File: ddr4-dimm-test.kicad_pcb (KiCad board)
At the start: 2 copper layers, 133.3 x 31.2 mm, 1 part

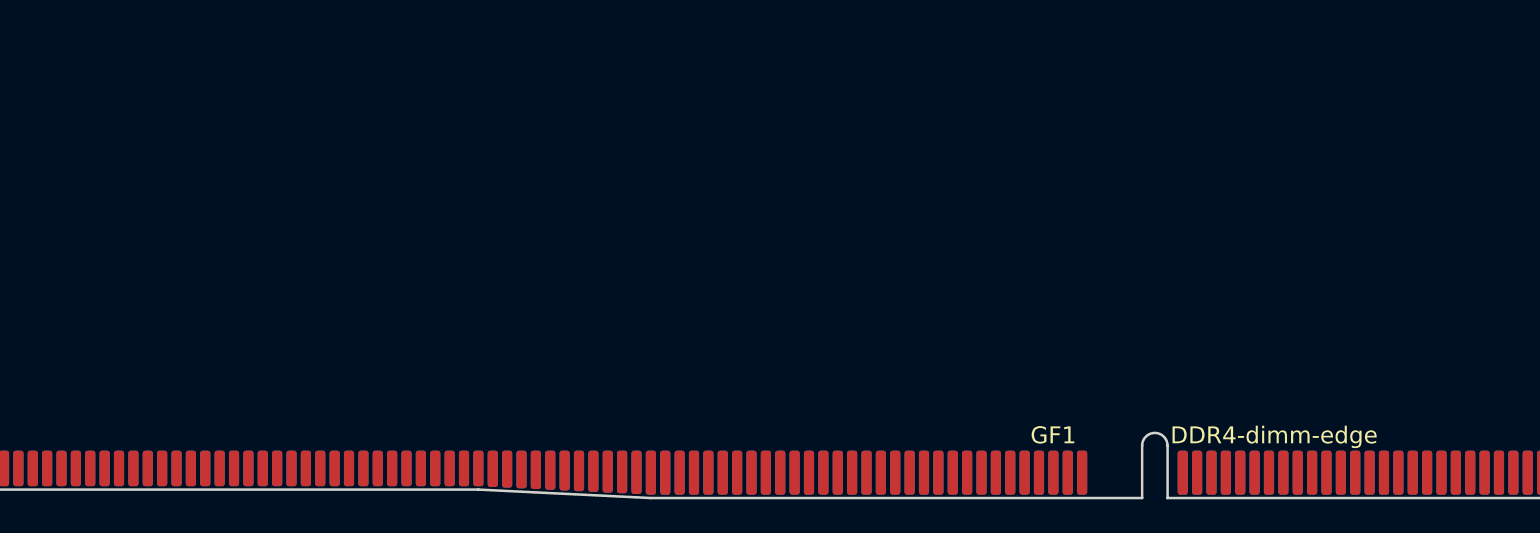
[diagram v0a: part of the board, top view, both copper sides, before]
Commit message: Added ram chip symbol and partial connections
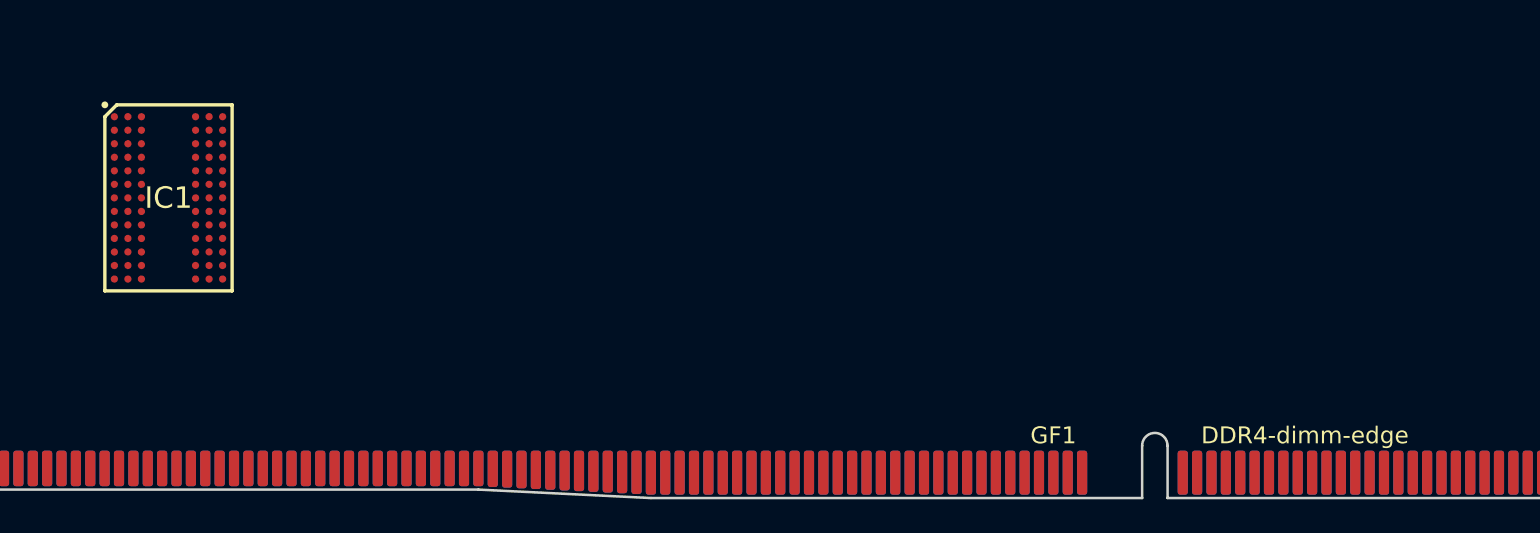
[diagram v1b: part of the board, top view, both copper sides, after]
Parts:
- added IC1: DDR4-BGA78, A_my_stuff:DDR4-BGA78, F.Cu at (89.3, 94.2)
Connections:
- GF1 pad 210: unconnected-(GF1-A11-Pad210) -> A11
- GF1 pad 211: unconnected-(GF1-A7-Pad211) -> A7
- GF1 pad 213: unconnected-(GF1-A5-Pad213) -> A5
- GF1 pad 214: unconnected-(GF1-A4-Pad214) -> A4
- GF1 pad 216: unconnected-(GF1-A2-Pad216) -> A2
- GF1 pad 224: unconnected-(GF1-BA1-Pad224) -> BA1
- GF1 pad 225: unconnected-(GF1-A10/AP-Pad225) -> A10
- GF1 pad 228: unconnected-(GF1-A14/WE#-Pad228) -> A14
- GF1 pad 232: unconnected-(GF1-A13-Pad232) -> A13
- GF1 pad 65: unconnected-(GF1-A12/BC#-Pad65) -> A12
- GF1 pad 66: unconnected-(GF1-A9-Pad66) -> A9
- GF1 pad 68: unconnected-(GF1-A8-Pad68) -> A8
- GF1 pad 69: unconnected-(GF1-A6-Pad69) -> A6
- GF1 pad 71: unconnected-(GF1-A3-Pad71) -> A3
- GF1 pad 72: unconnected-(GF1-A1-Pad72) -> A1
- GF1 pad 79: unconnected-(GF1-A0-Pad79) -> A0
- GF1 pad 81: unconnected-(GF1-BA0-Pad81) -> BA0
- GF1 pad 82: unconnected-(GF1-A16/RAS#-Pad82) -> A16
- GF1 pad 86: unconnected-(GF1-A15/CAS#-Pad86) -> A15

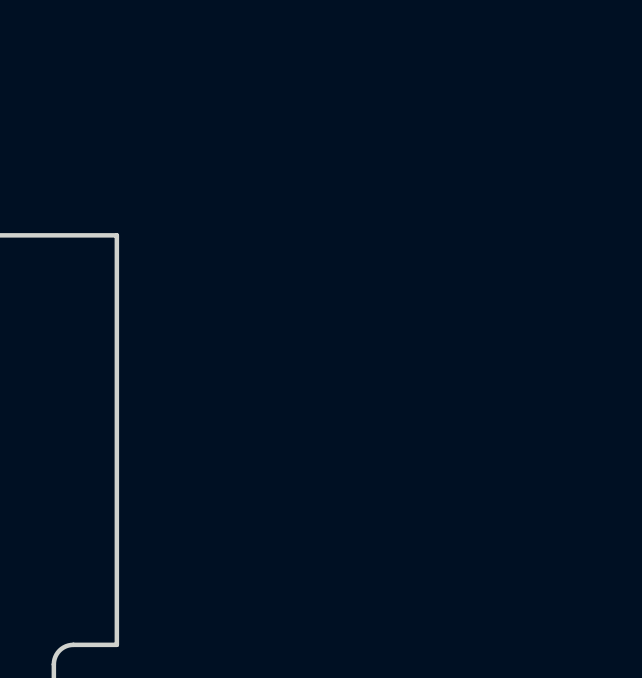
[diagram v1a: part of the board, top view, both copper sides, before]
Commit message: Connected all common lines and duplicated chip
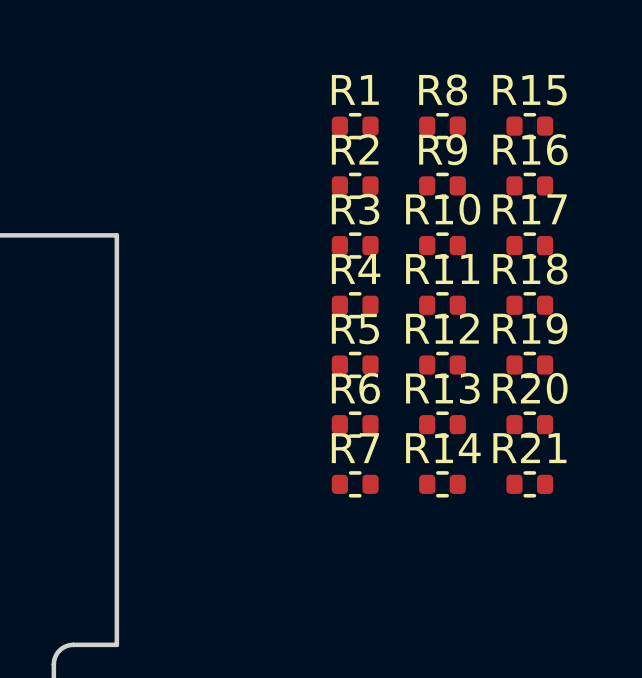
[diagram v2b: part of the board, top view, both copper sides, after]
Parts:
- added R1: 39Ω, Resistor_SMD:R_0402_1005Metric, F.Cu at (216.7, 77.1)
- added R10: 39Ω, Resistor_SMD:R_0402_1005Metric, F.Cu at (219.6, 81.0)
- added R11: 39Ω, Resistor_SMD:R_0402_1005Metric, F.Cu at (219.6, 83.0)
- added R12: 39Ω, Resistor_SMD:R_0402_1005Metric, F.Cu at (219.6, 85.0)
- added R13: 39Ω, Resistor_SMD:R_0402_1005Metric, F.Cu at (219.6, 87.0)
- added R14: 39Ω, Resistor_SMD:R_0402_1005Metric, F.Cu at (219.6, 89.0)
- added R15: 39Ω, Resistor_SMD:R_0402_1005Metric, F.Cu at (222.5, 77.1)
- added R16: 39Ω, Resistor_SMD:R_0402_1005Metric, F.Cu at (222.5, 79.0)
- added R17: 39Ω, Resistor_SMD:R_0402_1005Metric, F.Cu at (222.5, 81.0)
- added R18: 39Ω, Resistor_SMD:R_0402_1005Metric, F.Cu at (222.5, 83.0)
- added R19: 39Ω, Resistor_SMD:R_0402_1005Metric, F.Cu at (222.5, 85.0)
- added R2: 39Ω, Resistor_SMD:R_0402_1005Metric, F.Cu at (216.7, 79.0)
- added R20: 39Ω, Resistor_SMD:R_0402_1005Metric, F.Cu at (222.5, 87.0)
- added R21: 39Ω, Resistor_SMD:R_0402_1005Metric, F.Cu at (222.5, 89.0)
- added R3: 39Ω, Resistor_SMD:R_0402_1005Metric, F.Cu at (216.7, 81.0)
- added R4: 39Ω, Resistor_SMD:R_0402_1005Metric, F.Cu at (216.7, 83.0)
- added R5: 39Ω, Resistor_SMD:R_0402_1005Metric, F.Cu at (216.7, 85.0)
- added R6: 39Ω, Resistor_SMD:R_0402_1005Metric, F.Cu at (216.7, 87.0)
- added R7: 39Ω, Resistor_SMD:R_0402_1005Metric, F.Cu at (216.7, 89.0)
- added R8: 39Ω, Resistor_SMD:R_0402_1005Metric, F.Cu at (219.6, 77.1)
- added R9: 39Ω, Resistor_SMD:R_0402_1005Metric, F.Cu at (219.6, 79.0)
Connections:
- GF1 pad 146: unconnected-(GF1-VREFCA-Pad146) -> VREFCA
- GF1 pad 207: unconnected-(GF1-BG1-Pad207) -> BG1
- GF1 pad 63: unconnected-(GF1-BG0-Pad63) -> BG0
- GF1 pad 74: unconnected-(GF1-CK0+-Pad74) -> CK0+
- GF1 pad 75: unconnected-(GF1-CK0--Pad75) -> CK0-
- IC1 pad A1: unconnected-(IC1-VDD_1-PadA1) -> VDD
- IC1 pad A2: unconnected-(IC1-VSSQ_1-PadA2) -> GND
- IC1 pad A8: unconnected-(IC1-VSSQ_2-PadA8) -> GND
- IC1 pad A9: unconnected-(IC1-VSS_1-PadA9) -> GND
- IC1 pad B1: unconnected-(IC1-VPP_1-PadB1) -> VPP
- IC1 pad B2: unconnected-(IC1-VDDQ_1-PadB2) -> VDD
- IC1 pad B8: unconnected-(IC1-VDDQ_2-PadB8) -> VDD
- IC1 pad C1: unconnected-(IC1-VDDQ_3-PadC1) -> VDD
- IC1 pad C7: unconnected-(IC1-VDD_2-PadC7) -> VDD
- IC1 pad C8: unconnected-(IC1-VSS_2-PadC8) -> GND
- IC1 pad C9: unconnected-(IC1-VDDQ_4-PadC9) -> VDD
- IC1 pad D1: unconnected-(IC1-VSSQ_3-PadD1) -> GND
- IC1 pad D9: unconnected-(IC1-VSSQ_4-PadD9) -> GND
- IC1 pad E1: unconnected-(IC1-VSS_3-PadE1) -> GND
- IC1 pad E2: unconnected-(IC1-VDDQ_5-PadE2) -> VDD
- IC1 pad E8: unconnected-(IC1-VDDQ_6-PadE8) -> VDD
- IC1 pad E9: unconnected-(IC1-VSS_4-PadE9) -> GND
- IC1 pad F1: unconnected-(IC1-VDD_3-PadF1) -> VDD
- IC1 pad F7: unconnected-(IC1-CK+-PadF7) -> CK0+
- IC1 pad F8: unconnected-(IC1-CK--PadF8) -> CK0-
- IC1 pad F9: unconnected-(IC1-VDD_4-PadF9) -> VDD
- IC1 pad G1: unconnected-(IC1-VSS_5-PadG1) -> GND
- IC1 pad H1: unconnected-(IC1-VDD_5-PadH1) -> VDD
- IC1 pad H9: unconnected-(IC1-VSS_6-PadH9) -> GND
- IC1 pad J1: unconnected-(IC1-VREFCA-PadJ1) -> VREFCA
- IC1 pad J2: unconnected-(IC1-BG0-PadJ2) -> BG0
- IC1 pad J8: unconnected-(IC1-BG1-PadJ8) -> BG1
- IC1 pad J9: unconnected-(IC1-VDD_6-PadJ9) -> VDD
- IC1 pad K1: unconnected-(IC1-VSS_7-PadK1) -> GND
- IC1 pad K9: unconnected-(IC1-VSS_8-PadK9) -> GND
- IC1 pad M1: unconnected-(IC1-VDD_7-PadM1) -> VDD
- IC1 pad M9: unconnected-(IC1-VPP_2-PadM9) -> VPP
- IC1 pad N1: unconnected-(IC1-VSS_9-PadN1) -> GND
- IC1 pad N9: unconnected-(IC1-VDD_8-PadN9) -> VDD

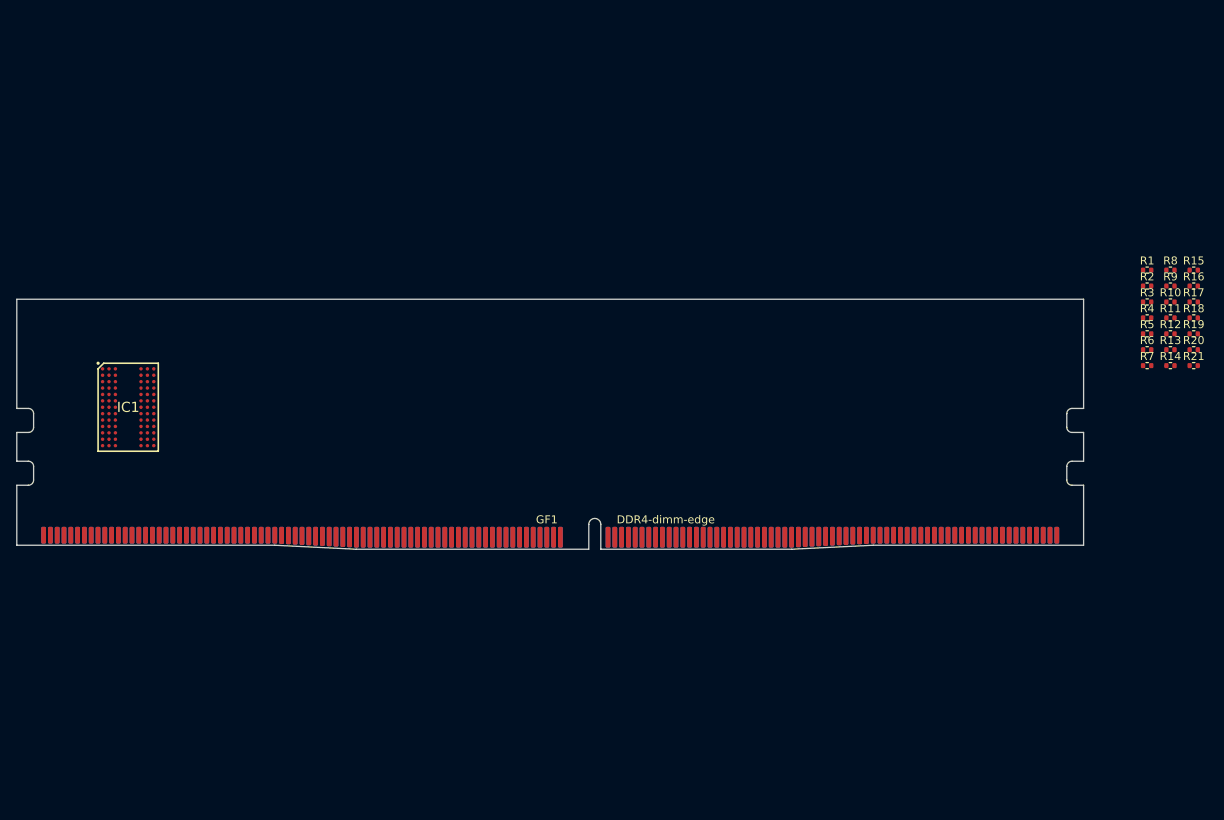
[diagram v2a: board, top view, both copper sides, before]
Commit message: Connected data bus
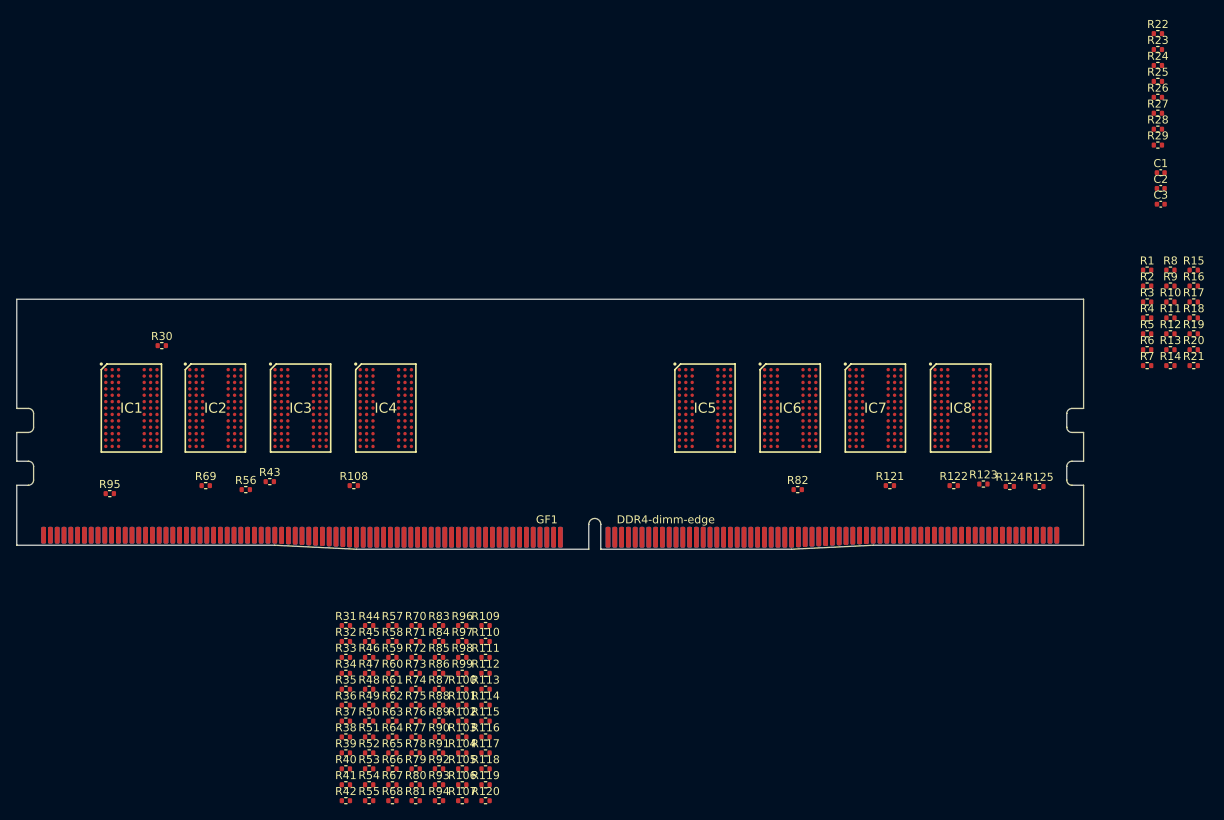
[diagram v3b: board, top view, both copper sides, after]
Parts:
- added C1: 0.01uF, Capacitor_SMD:C_0402_1005Metric, F.Cu at (218.4, 64.9)
- added C2: ?, Capacitor_SMD:C_0402_1005Metric, F.Cu at (218.4, 66.8)
- added C3: 10pF, Capacitor_SMD:C_0402_1005Metric, F.Cu at (218.4, 68.8)
- added IC2: DDR4-BGA78, A_my_stuff:DDR4-BGA78, F.Cu at (100.2, 94.3)
- added IC3: DDR4-BGA78, A_my_stuff:DDR4-BGA78, F.Cu at (110.8, 94.3)
- added IC4: DDR4-BGA78, A_my_stuff:DDR4-BGA78, F.Cu at (121.5, 94.3)
- added IC5: DDR4-BGA78, A_my_stuff:DDR4-BGA78, F.Cu at (161.4, 94.3)
- added IC6: DDR4-BGA78, A_my_stuff:DDR4-BGA78, F.Cu at (172.1, 94.3)
- added IC7: DDR4-BGA78, A_my_stuff:DDR4-BGA78, F.Cu at (182.7, 94.3)
- added IC8: DDR4-BGA78, A_my_stuff:DDR4-BGA78, F.Cu at (193.3, 94.3)
- added R100: 15Ω, Resistor_SMD:R_0402_1005Metric, F.Cu at (131.1, 129.4)
- added R101: 15Ω, Resistor_SMD:R_0402_1005Metric, F.Cu at (131.1, 131.4)
- added R102: 15Ω, Resistor_SMD:R_0402_1005Metric, F.Cu at (131.1, 133.4)
- added R103: 15Ω, Resistor_SMD:R_0402_1005Metric, F.Cu at (131.1, 135.4)
- added R104: 15Ω, Resistor_SMD:R_0402_1005Metric, F.Cu at (131.1, 137.4)
- added R105: 15Ω, Resistor_SMD:R_0402_1005Metric, F.Cu at (131.1, 139.4)
- added R106: 15Ω, Resistor_SMD:R_0402_1005Metric, F.Cu at (131.1, 141.4)
- added R107: 15Ω, Resistor_SMD:R_0402_1005Metric, F.Cu at (131.1, 143.4)
- added R108: 15Ω, Resistor_SMD:R_0402_1005Metric, F.Cu at (117.5, 104.0)
- added R109: 15Ω, Resistor_SMD:R_0402_1005Metric, F.Cu at (134.0, 121.5)
- added R110: 15Ω, Resistor_SMD:R_0402_1005Metric, F.Cu at (134.0, 123.5)
- added R111: 15Ω, Resistor_SMD:R_0402_1005Metric, F.Cu at (134.0, 125.5)
- added R112: 15Ω, Resistor_SMD:R_0402_1005Metric, F.Cu at (134.0, 127.5)
- added R113: 15Ω, Resistor_SMD:R_0402_1005Metric, F.Cu at (134.0, 129.4)
- added R114: 15Ω, Resistor_SMD:R_0402_1005Metric, F.Cu at (134.0, 131.4)
- added R115: 15Ω, Resistor_SMD:R_0402_1005Metric, F.Cu at (134.0, 133.4)
- added R116: 15Ω, Resistor_SMD:R_0402_1005Metric, F.Cu at (134.0, 135.4)
- added R117: 15Ω, Resistor_SMD:R_0402_1005Metric, F.Cu at (134.0, 137.4)
- added R118: 15Ω, Resistor_SMD:R_0402_1005Metric, F.Cu at (134.0, 139.4)
- added R119: 15Ω, Resistor_SMD:R_0402_1005Metric, F.Cu at (134.0, 141.4)
- added R120: 15Ω, Resistor_SMD:R_0402_1005Metric, F.Cu at (134.0, 143.4)
- added R121: 15Ω, Resistor_SMD:R_0402_1005Metric, F.Cu at (184.5, 104.0)
- added R122: 15Ω, Resistor_SMD:R_0402_1005Metric, F.Cu at (192.5, 104.0)
- added R123: 15Ω, Resistor_SMD:R_0402_1005Metric, F.Cu at (196.2, 103.8)
- added R124: 15Ω, Resistor_SMD:R_0402_1005Metric, F.Cu at (199.5, 104.1)
- added R125: 15Ω, Resistor_SMD:R_0402_1005Metric, F.Cu at (203.2, 104.1)
- added R22: 39Ω, Resistor_SMD:R_0402_1005Metric, F.Cu at (218.0, 47.5)
- added R23: 39Ω, Resistor_SMD:R_0402_1005Metric, F.Cu at (218.0, 49.5)
- added R24: 39Ω, Resistor_SMD:R_0402_1005Metric, F.Cu at (218.0, 51.5)
- added R25: 39Ω, Resistor_SMD:R_0402_1005Metric, F.Cu at (218.0, 53.5)
- added R26: 39Ω, Resistor_SMD:R_0402_1005Metric, F.Cu at (218.0, 55.5)
- added R27: 39Ω, Resistor_SMD:R_0402_1005Metric, F.Cu at (218.0, 57.5)
- added R28: 39Ω, Resistor_SMD:R_0402_1005Metric, F.Cu at (218.0, 59.4)
- added R29: 47Ω, Resistor_SMD:R_0402_1005Metric, F.Cu at (218.0, 61.4)
- added R30: 240Ω, Resistor_SMD:R_0402_1005Metric, F.Cu at (93.5, 86.5)
- added R31: 240Ω, Resistor_SMD:R_0402_1005Metric, F.Cu at (116.5, 121.5)
- added R32: 240Ω, Resistor_SMD:R_0402_1005Metric, F.Cu at (116.5, 123.5)
- added R33: 240Ω, Resistor_SMD:R_0402_1005Metric, F.Cu at (116.5, 125.5)
- added R34: 240Ω, Resistor_SMD:R_0402_1005Metric, F.Cu at (116.5, 127.5)
- added R35: 240Ω, Resistor_SMD:R_0402_1005Metric, F.Cu at (116.5, 129.4)
- added R36: 240Ω, Resistor_SMD:R_0402_1005Metric, F.Cu at (116.5, 131.4)
- added R37: 240Ω, Resistor_SMD:R_0402_1005Metric, F.Cu at (116.5, 133.4)
- added R38: 15Ω, Resistor_SMD:R_0402_1005Metric, F.Cu at (116.5, 135.4)
- added R39: 15Ω, Resistor_SMD:R_0402_1005Metric, F.Cu at (116.5, 137.4)
- added R40: 15Ω, Resistor_SMD:R_0402_1005Metric, F.Cu at (116.5, 139.4)
- added R41: 15Ω, Resistor_SMD:R_0402_1005Metric, F.Cu at (116.5, 141.4)
- added R42: 15Ω, Resistor_SMD:R_0402_1005Metric, F.Cu at (116.5, 143.4)
- added R43: 15Ω, Resistor_SMD:R_0402_1005Metric, F.Cu at (107.0, 103.5)
- added R44: 15Ω, Resistor_SMD:R_0402_1005Metric, F.Cu at (119.4, 121.5)
- added R45: 15Ω, Resistor_SMD:R_0402_1005Metric, F.Cu at (119.4, 123.5)
- added R46: 15Ω, Resistor_SMD:R_0402_1005Metric, F.Cu at (119.4, 125.5)
- added R47: 15Ω, Resistor_SMD:R_0402_1005Metric, F.Cu at (119.4, 127.5)
- added R48: 15Ω, Resistor_SMD:R_0402_1005Metric, F.Cu at (119.4, 129.4)
- added R49: 15Ω, Resistor_SMD:R_0402_1005Metric, F.Cu at (119.4, 131.4)
- added R50: 15Ω, Resistor_SMD:R_0402_1005Metric, F.Cu at (119.4, 133.4)
- added R51: 15Ω, Resistor_SMD:R_0402_1005Metric, F.Cu at (119.4, 135.4)
- added R52: 15Ω, Resistor_SMD:R_0402_1005Metric, F.Cu at (119.4, 137.4)
- added R53: 15Ω, Resistor_SMD:R_0402_1005Metric, F.Cu at (119.4, 139.4)
- added R54: 15Ω, Resistor_SMD:R_0402_1005Metric, F.Cu at (119.4, 141.4)
- added R55: 15Ω, Resistor_SMD:R_0402_1005Metric, F.Cu at (119.4, 143.4)
- added R56: 15Ω, Resistor_SMD:R_0402_1005Metric, F.Cu at (104.0, 104.5)
- added R57: 15Ω, Resistor_SMD:R_0402_1005Metric, F.Cu at (122.3, 121.5)
- added R58: 15Ω, Resistor_SMD:R_0402_1005Metric, F.Cu at (122.3, 123.5)
- added R59: 15Ω, Resistor_SMD:R_0402_1005Metric, F.Cu at (122.3, 125.5)
- added R60: 15Ω, Resistor_SMD:R_0402_1005Metric, F.Cu at (122.3, 127.5)
- added R61: 15Ω, Resistor_SMD:R_0402_1005Metric, F.Cu at (122.3, 129.4)
- added R62: 15Ω, Resistor_SMD:R_0402_1005Metric, F.Cu at (122.3, 131.4)
- added R63: 15Ω, Resistor_SMD:R_0402_1005Metric, F.Cu at (122.3, 133.4)
- added R64: 15Ω, Resistor_SMD:R_0402_1005Metric, F.Cu at (122.3, 135.4)
- added R65: 15Ω, Resistor_SMD:R_0402_1005Metric, F.Cu at (122.3, 137.4)
- added R66: 15Ω, Resistor_SMD:R_0402_1005Metric, F.Cu at (122.3, 139.4)
- added R67: 15Ω, Resistor_SMD:R_0402_1005Metric, F.Cu at (122.3, 141.4)
- added R68: 15Ω, Resistor_SMD:R_0402_1005Metric, F.Cu at (122.3, 143.4)
- added R69: 15Ω, Resistor_SMD:R_0402_1005Metric, F.Cu at (99.0, 104.0)
- added R70: 15Ω, Resistor_SMD:R_0402_1005Metric, F.Cu at (125.2, 121.5)
- added R71: 15Ω, Resistor_SMD:R_0402_1005Metric, F.Cu at (125.2, 123.5)
- added R72: 15Ω, Resistor_SMD:R_0402_1005Metric, F.Cu at (125.2, 125.5)
- added R73: 15Ω, Resistor_SMD:R_0402_1005Metric, F.Cu at (125.2, 127.5)
- added R74: 15Ω, Resistor_SMD:R_0402_1005Metric, F.Cu at (125.2, 129.4)
- added R75: 15Ω, Resistor_SMD:R_0402_1005Metric, F.Cu at (125.2, 131.4)
- added R76: 15Ω, Resistor_SMD:R_0402_1005Metric, F.Cu at (125.2, 133.4)
- added R77: 15Ω, Resistor_SMD:R_0402_1005Metric, F.Cu at (125.2, 135.4)
- added R78: 15Ω, Resistor_SMD:R_0402_1005Metric, F.Cu at (125.2, 137.4)
- added R79: 15Ω, Resistor_SMD:R_0402_1005Metric, F.Cu at (125.2, 139.4)
- added R80: 15Ω, Resistor_SMD:R_0402_1005Metric, F.Cu at (125.2, 141.4)
- added R81: 15Ω, Resistor_SMD:R_0402_1005Metric, F.Cu at (125.2, 143.4)
- added R82: 15Ω, Resistor_SMD:R_0402_1005Metric, F.Cu at (173.0, 104.5)
- added R83: 15Ω, Resistor_SMD:R_0402_1005Metric, F.Cu at (128.2, 121.5)
- added R84: 15Ω, Resistor_SMD:R_0402_1005Metric, F.Cu at (128.2, 123.5)
- added R85: 15Ω, Resistor_SMD:R_0402_1005Metric, F.Cu at (128.2, 125.5)
- added R86: 15Ω, Resistor_SMD:R_0402_1005Metric, F.Cu at (128.2, 127.5)
- added R87: 15Ω, Resistor_SMD:R_0402_1005Metric, F.Cu at (128.2, 129.4)
- added R88: 15Ω, Resistor_SMD:R_0402_1005Metric, F.Cu at (128.2, 131.4)
- added R89: 15Ω, Resistor_SMD:R_0402_1005Metric, F.Cu at (128.2, 133.4)
- added R90: 15Ω, Resistor_SMD:R_0402_1005Metric, F.Cu at (128.2, 135.4)
- added R91: 15Ω, Resistor_SMD:R_0402_1005Metric, F.Cu at (128.2, 137.4)
- added R92: 15Ω, Resistor_SMD:R_0402_1005Metric, F.Cu at (128.2, 139.4)
- added R93: 15Ω, Resistor_SMD:R_0402_1005Metric, F.Cu at (128.2, 141.4)
- added R94: 15Ω, Resistor_SMD:R_0402_1005Metric, F.Cu at (128.2, 143.4)
- added R95: 15Ω, Resistor_SMD:R_0402_1005Metric, F.Cu at (87.0, 105.0)
- added R96: 15Ω, Resistor_SMD:R_0402_1005Metric, F.Cu at (131.1, 121.5)
- added R97: 15Ω, Resistor_SMD:R_0402_1005Metric, F.Cu at (131.1, 123.5)
- added R98: 15Ω, Resistor_SMD:R_0402_1005Metric, F.Cu at (131.1, 125.5)
- added R99: 15Ω, Resistor_SMD:R_0402_1005Metric, F.Cu at (131.1, 127.5)
- moved IC1 0.41 mm to (89.7, 94.3)
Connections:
- GF1 pad 10: unconnected-(GF1-DQ6-Pad10) -> Net-(GF1-DQ6)
- GF1 pad 102: unconnected-(GF1-DQ38-Pad102) -> Net-(GF1-DQ38)
- GF1 pad 104: unconnected-(GF1-DQ34-Pad104) -> Net-(GF1-DQ34)
- GF1 pad 106: unconnected-(GF1-DQ44-Pad106) -> Net-(GF1-DQ44)
- GF1 pad 108: unconnected-(GF1-DQ40-Pad108) -> Net-(GF1-DQ40)
- GF1 pad 110: unconnected-(GF1-(T)DQS14+-Pad110) -> /R_DM5
- GF1 pad 113: unconnected-(GF1-DQ46-Pad113) -> Net-(GF1-DQ46)
- GF1 pad 115: unconnected-(GF1-DQ42-Pad115) -> Net-(GF1-DQ42)
- GF1 pad 117: unconnected-(GF1-DQ52-Pad117) -> Net-(GF1-DQ52)
- GF1 pad 119: unconnected-(GF1-DQ48-Pad119) -> Net-(GF1-DQ48)
- GF1 pad 12: unconnected-(GF1-DQ2-Pad12) -> Net-(GF1-DQ2)
- GF1 pad 121: unconnected-(GF1-(T)DQS15+-Pad121) -> /R_DM6
- GF1 pad 124: unconnected-(GF1-DQ54-Pad124) -> Net-(GF1-DQ54)
- GF1 pad 126: unconnected-(GF1-DQ50-Pad126) -> Net-(GF1-DQ50)
- GF1 pad 128: unconnected-(GF1-DQ60-Pad128) -> Net-(GF1-DQ60)
- GF1 pad 130: unconnected-(GF1-DQ56-Pad130) -> Net-(GF1-DQ56)
- GF1 pad 132: unconnected-(GF1-(T)DQS16+-Pad132) -> /R_DM7
- GF1 pad 135: unconnected-(GF1-DQ62-Pad135) -> Net-(GF1-DQ62)
- GF1 pad 137: unconnected-(GF1-DQ58-Pad137) -> Net-(GF1-DQ58)
- GF1 pad 14: unconnected-(GF1-DQ12-Pad14) -> Net-(GF1-DQ12)
- GF1 pad 148: unconnected-(GF1-DQ5-Pad148) -> Net-(GF1-DQ5)
- GF1 pad 150: unconnected-(GF1-DQ1-Pad150) -> Net-(GF1-DQ1)
- GF1 pad 152: unconnected-(GF1-DQS0--Pad152) -> /R_DQS0-
- GF1 pad 153: unconnected-(GF1-DQS0+-Pad153) -> /R_DQS0+
- GF1 pad 155: unconnected-(GF1-DQ7-Pad155) -> Net-(GF1-DQ7)
- GF1 pad 157: unconnected-(GF1-DQ3-Pad157) -> Net-(GF1-DQ3)
- GF1 pad 159: unconnected-(GF1-DQ13-Pad159) -> Net-(GF1-DQ13)
- GF1 pad 16: unconnected-(GF1-DQ8-Pad16) -> Net-(GF1-DQ8)
- GF1 pad 161: unconnected-(GF1-DQ9-Pad161) -> Net-(GF1-DQ9)
- GF1 pad 163: unconnected-(GF1-DQS1--Pad163) -> /R_DQS1-
- GF1 pad 164: unconnected-(GF1-DQS1+-Pad164) -> /R_DQS1+
- GF1 pad 166: unconnected-(GF1-DQ15-Pad166) -> Net-(GF1-DQ15)
- GF1 pad 168: unconnected-(GF1-DQ11-Pad168) -> Net-(GF1-DQ11)
- GF1 pad 170: unconnected-(GF1-DQ21-Pad170) -> Net-(GF1-DQ21)
- GF1 pad 172: unconnected-(GF1-DQ17-Pad172) -> Net-(GF1-DQ17)
- GF1 pad 174: unconnected-(GF1-DQS2--Pad174) -> /R_DQS2-
- GF1 pad 175: unconnected-(GF1-DQS2+-Pad175) -> /R_DQS2+
- GF1 pad 177: unconnected-(GF1-DQ23-Pad177) -> Net-(GF1-DQ23)
- GF1 pad 179: unconnected-(GF1-DQ19-Pad179) -> Net-(GF1-DQ19)
- GF1 pad 18: unconnected-(GF1-(T)DQS10+-Pad18) -> /R_DM1
- GF1 pad 181: unconnected-(GF1-DQ29-Pad181) -> Net-(GF1-DQ29)
- GF1 pad 183: unconnected-(GF1-DQ25-Pad183) -> Net-(GF1-DQ25)
- GF1 pad 185: unconnected-(GF1-DQS3--Pad185) -> /R_DQS3-
- GF1 pad 186: unconnected-(GF1-DQS3+-Pad186) -> /R_DQS3+
- GF1 pad 188: unconnected-(GF1-DQ31-Pad188) -> Net-(GF1-DQ31)
- GF1 pad 190: unconnected-(GF1-DQ27-Pad190) -> Net-(GF1-DQ27)
- GF1 pad 208: unconnected-(GF1-ALERT#-Pad208) -> ALERT#
- GF1 pad 21: unconnected-(GF1-DQ14-Pad21) -> Net-(GF1-DQ14)
- GF1 pad 222: unconnected-(GF1-PARITY-Pad222) -> PARITY
- GF1 pad 23: unconnected-(GF1-DQ10-Pad23) -> Net-(GF1-DQ10)
- GF1 pad 240: unconnected-(GF1-DQ37-Pad240) -> Net-(GF1-DQ37)
- GF1 pad 242: unconnected-(GF1-DQ33-Pad242) -> Net-(GF1-DQ33)
- GF1 pad 244: unconnected-(GF1-DQS4--Pad244) -> /R_DQS4-
- GF1 pad 245: unconnected-(GF1-DQS4+-Pad245) -> /R_DQS4+
- GF1 pad 247: unconnected-(GF1-DQ39-Pad247) -> Net-(GF1-DQ39)
- GF1 pad 249: unconnected-(GF1-DQ35-Pad249) -> Net-(GF1-DQ35)
- GF1 pad 25: unconnected-(GF1-DQ20-Pad25) -> Net-(GF1-DQ20)
- GF1 pad 251: unconnected-(GF1-DQ45-Pad251) -> Net-(GF1-DQ45)
- GF1 pad 253: unconnected-(GF1-DQ41-Pad253) -> Net-(GF1-DQ41)
- GF1 pad 255: unconnected-(GF1-DQS5--Pad255) -> /R_DQS5-
- GF1 pad 256: unconnected-(GF1-DQS5+-Pad256) -> /R_DQS5+
- GF1 pad 258: unconnected-(GF1-DQ47-Pad258) -> Net-(GF1-DQ47)
- GF1 pad 260: unconnected-(GF1-DQ43-Pad260) -> Net-(GF1-DQ43)
- GF1 pad 262: unconnected-(GF1-DQ53-Pad262) -> Net-(GF1-DQ53)
- GF1 pad 264: unconnected-(GF1-DQ49-Pad264) -> Net-(GF1-DQ49)
- GF1 pad 266: unconnected-(GF1-DQS6--Pad266) -> /R_DQS6-
- GF1 pad 267: unconnected-(GF1-DQS6+-Pad267) -> /R_DQS6+
- GF1 pad 269: unconnected-(GF1-DQ55-Pad269) -> Net-(GF1-DQ55)
- GF1 pad 27: unconnected-(GF1-DQ16-Pad27) -> Net-(GF1-DQ16)
- GF1 pad 271: unconnected-(GF1-DQ51-Pad271) -> Net-(GF1-DQ51)
- GF1 pad 273: unconnected-(GF1-DQ61-Pad273) -> Net-(GF1-DQ61)
- GF1 pad 275: unconnected-(GF1-DQ57-Pad275) -> Net-(GF1-DQ57)
- GF1 pad 277: unconnected-(GF1-DQS7--Pad277) -> /R_DQS7-
- GF1 pad 278: unconnected-(GF1-DQS7+-Pad278) -> /R_DQS7+
- GF1 pad 280: unconnected-(GF1-DQ63-Pad280) -> Net-(GF1-DQ63)
- GF1 pad 282: unconnected-(GF1-DQ59-Pad282) -> Net-(GF1-DQ59)
- GF1 pad 29: unconnected-(GF1-(T)DQS11+-Pad29) -> /R_DM2
- GF1 pad 3: unconnected-(GF1-DQ4-Pad3) -> Net-(GF1-DQ4)
- GF1 pad 32: unconnected-(GF1-DQ22-Pad32) -> Net-(GF1-DQ22)
- GF1 pad 34: unconnected-(GF1-DQ18-Pad34) -> Net-(GF1-DQ18)
- GF1 pad 36: unconnected-(GF1-DQ28-Pad36) -> Net-(GF1-DQ28)
- GF1 pad 38: unconnected-(GF1-DQ24-Pad38) -> Net-(GF1-DQ24)
- GF1 pad 40: unconnected-(GF1-(T)DQS12+-Pad40) -> /R_DM3
- GF1 pad 43: unconnected-(GF1-DQ30-Pad43) -> Net-(GF1-DQ30)
- GF1 pad 45: unconnected-(GF1-DQ26-Pad45) -> Net-(GF1-DQ26)
- GF1 pad 5: unconnected-(GF1-DQ0-Pad5) -> Net-(GF1-DQ0)
- GF1 pad 58: unconnected-(GF1-RESET#-Pad58) -> RESET#
- GF1 pad 60: unconnected-(GF1-CKE0-Pad60) -> CKE0
- GF1 pad 62: unconnected-(GF1-ACT#-Pad62) -> ACT#
- GF1 pad 7: unconnected-(GF1-(T)DQS9+-Pad7) -> /R_DM0
- GF1 pad 84: unconnected-(GF1-CS0#-Pad84) -> CS0#
- GF1 pad 87: unconnected-(GF1-ODT0-Pad87) -> ODT0
- GF1 pad 95: unconnected-(GF1-DQ36-Pad95) -> Net-(GF1-DQ36)
- GF1 pad 97: unconnected-(GF1-DQ32-Pad97) -> Net-(GF1-DQ32)
- GF1 pad 99: unconnected-(GF1-(T)DQS13+-Pad99) -> /R_DM4
- IC1 pad A7: unconnected-(IC1-NFNF/DM_N/DBI_N/TDQS_T-PadA7) -> DM0
- IC1 pad B3: unconnected-(IC1-DQS_C-PadB3) -> DQS0-
- IC1 pad B7: unconnected-(IC1-DQ1-PadB7) -> DQ1
- IC1 pad B9: unconnected-(IC1-ZQ-PadB9) -> Net-(IC1-ZQ)
- IC1 pad C2: unconnected-(IC1-DQ0-PadC2) -> DQ0
- IC1 pad C3: unconnected-(IC1-DQS_T-PadC3) -> DQS0+
- IC1 pad D2: unconnected-(IC1-DQ4-PadD2) -> DQ4
- IC1 pad D3: unconnected-(IC1-DQ2-PadD3) -> DQ2
- IC1 pad D7: unconnected-(IC1-DQ3-PadD7) -> DQ3
- IC1 pad D8: unconnected-(IC1-DQ5-PadD8) -> DQ5
- IC1 pad E3: unconnected-(IC1-DQ6-PadE3) -> DQ6
- IC1 pad E7: unconnected-(IC1-DQ7-PadE7) -> DQ7
- IC1 pad F3: unconnected-(IC1-ODT-PadF3) -> ODT0
- IC1 pad G3: unconnected-(IC1-CKE-PadG3) -> CKE0
- IC1 pad G7: unconnected-(IC1-CS#-PadG7) -> CS0#
- IC1 pad H3: unconnected-(IC1-ACT_N-PadH3) -> ACT#
- IC1 pad L1: unconnected-(IC1-RESET#-PadL1) -> RESET#
- IC1 pad L9: unconnected-(IC1-ALERT_N-PadL9) -> ALERT#
- IC1 pad N3: unconnected-(IC1-PAR-PadN3) -> PARITY
